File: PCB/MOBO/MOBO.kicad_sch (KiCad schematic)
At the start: 10 parts, among them J101 COMP_OUT, J102 COMP_5V, J103 COMP_GND, J104 RPi_GPio, J105 JST_02, J106 RPi_SDA0, J107 RPi_TV, J108 RPi_D-, J109 RPi_D+, J110 RPi_SCL0

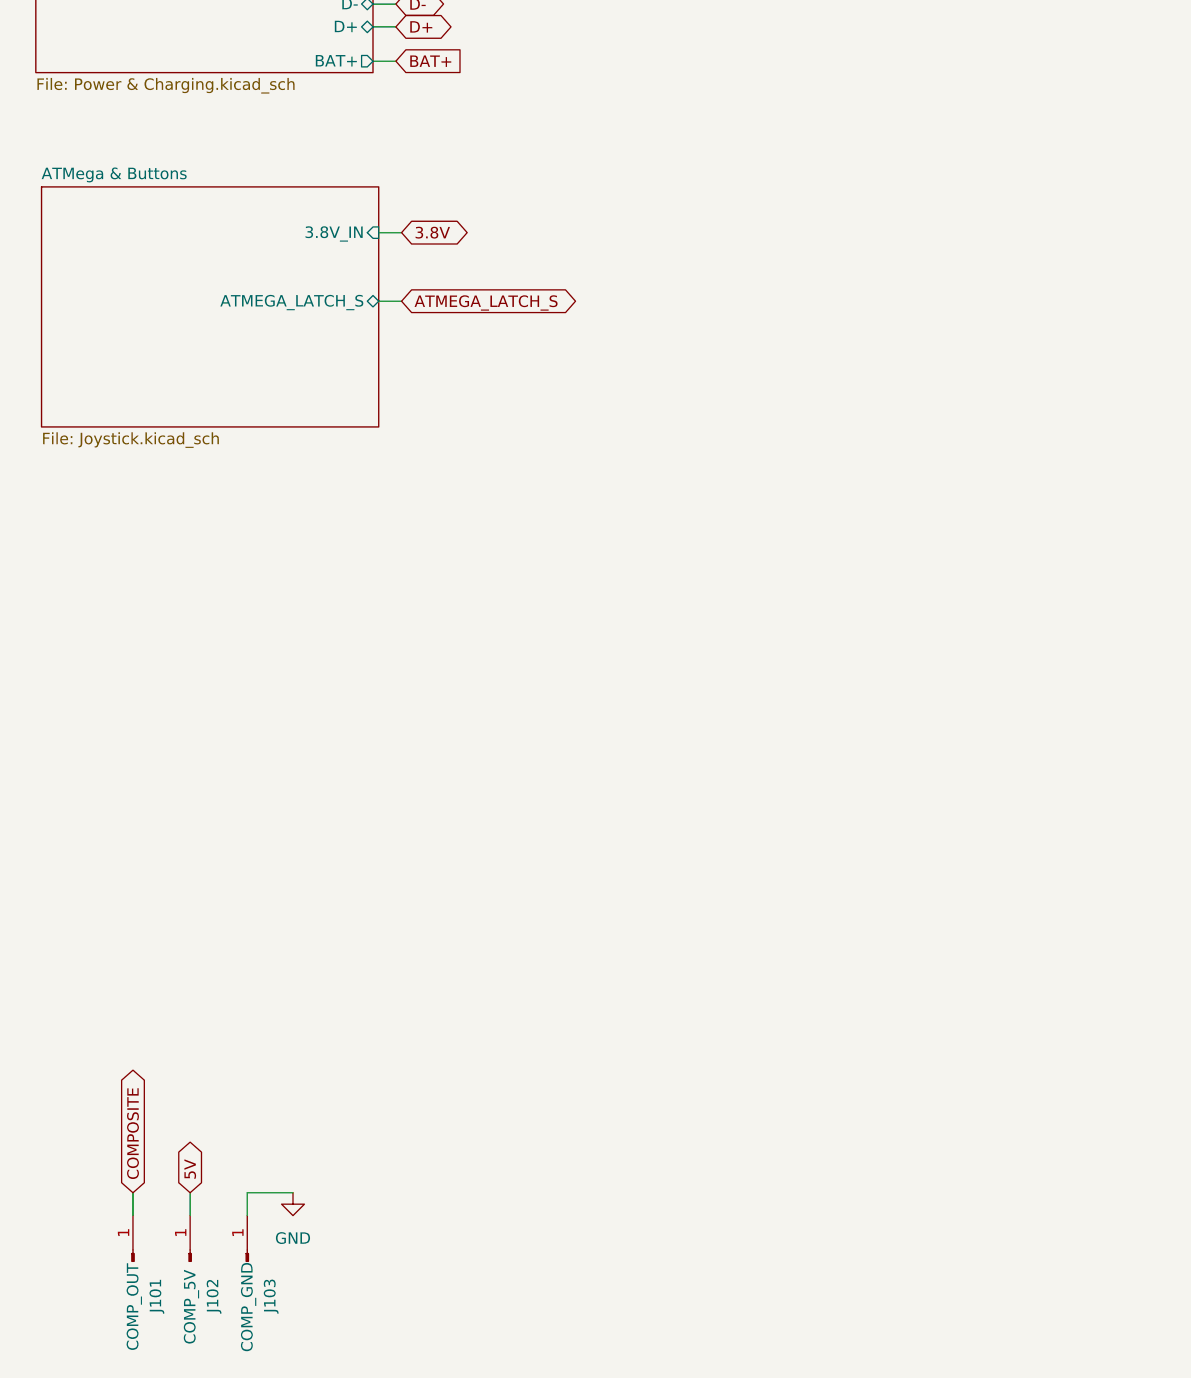
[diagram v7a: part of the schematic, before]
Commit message: schematic cleanup Added:  - Power flags  - Fixed loose connections
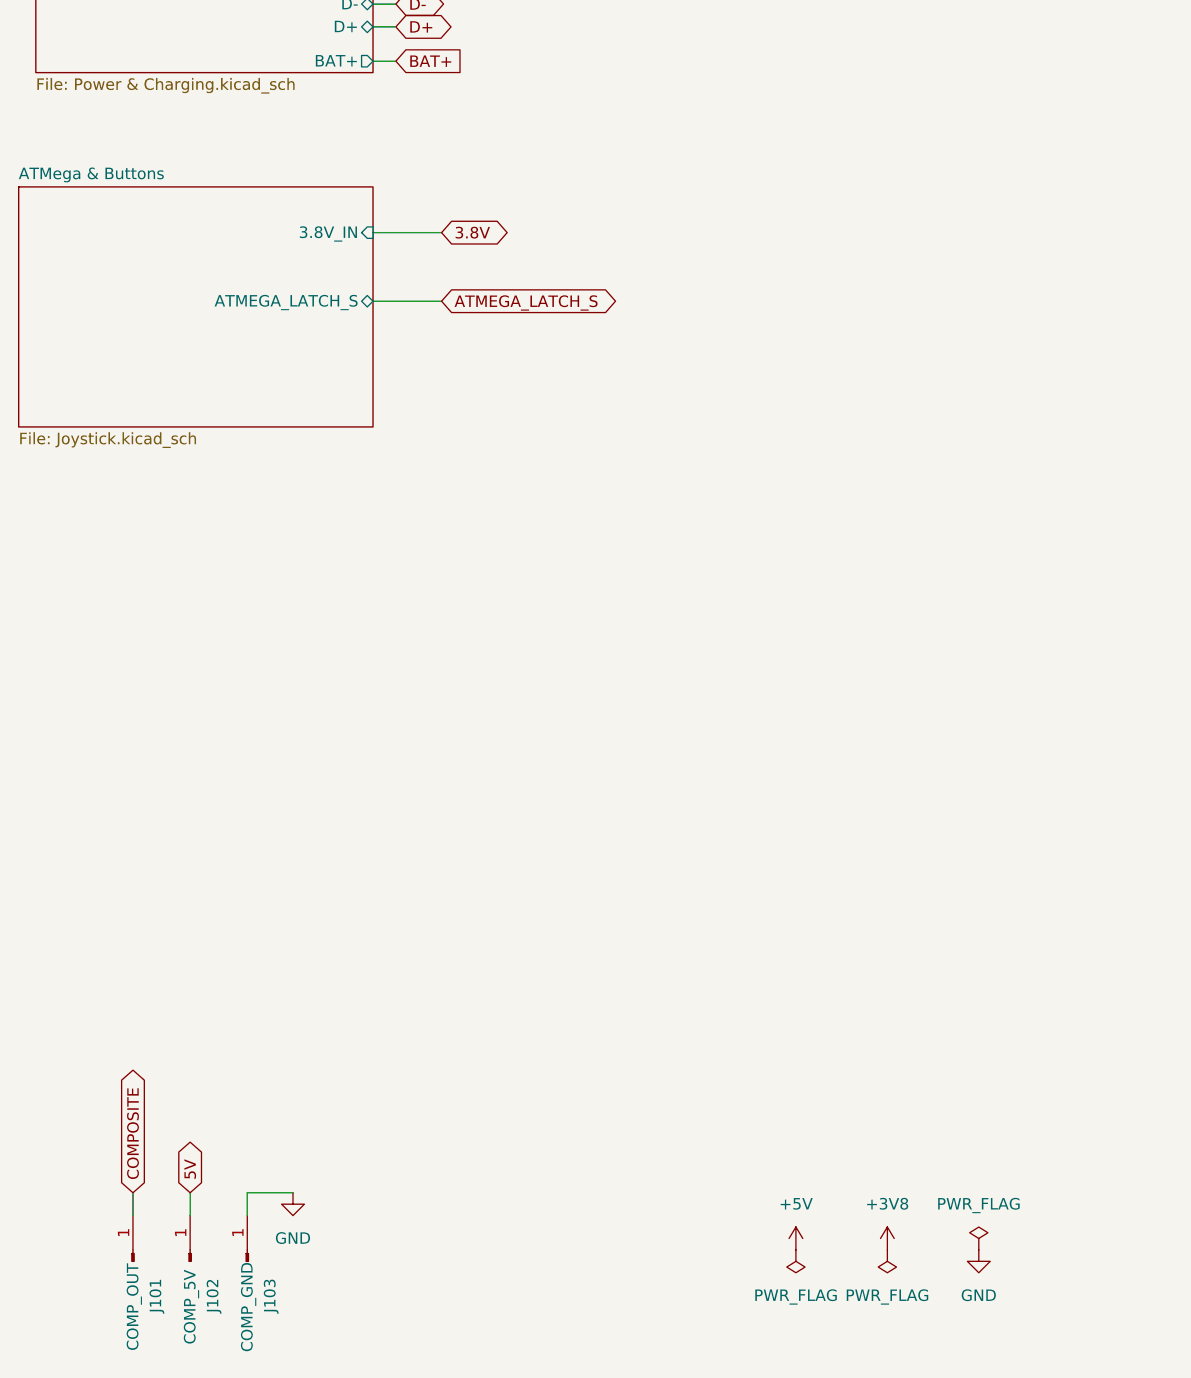
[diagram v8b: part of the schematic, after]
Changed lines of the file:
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@@
     (stroke (width 0) (type default))
   )
-  (wire (pts (xy 60.325 76.2) (xy 62.865 76.2))
+  (wire (pts (xy 59.69 76.2) (xy 67.31 76.2))
     (stroke (width 0) (type default))
   )
@@
     (stroke (width 0) (type default))
   )
-  (wire (pts (xy 60.325 68.58) (xy 62.865 68.58))
+  (wire (pts (xy 59.69 68.58) (xy 67.31 68.58))
     (stroke (width 0) (type default))
   )
@@
     )
   )
-  (global_label "ATMEGA_LATCH_S" (shape bidirectional) (at 62.865 76.2 0) (fields_autoplaced)
-    (effects (font (size 1.27 1.27)) (justify left))
-    (property "Intersheetrefs" "${INTERSHEET_REFS}" (at 82.8062 76.2 0)
+  (global_label "ATMEGA_LATCH_S" (shape bidirectional) (at 67.31 76.2 0) (fields_autoplaced)
+    (effects (font (size 1.27 1.27)) (justify left))
+    (property "Intersheetrefs" "${INTERSHEET_REFS}" (at 87.2512 76.2 0)
       (effects (font (size 1.27 1.27)) (justify left) hide)
     )
@@
     )
   )
-  (global_label "3.8V" (shape bidirectional) (at 62.865 68.58 0) (fields_autoplaced)
-    (effects (font (size 1.27 1.27)) (justify left))
-    (property "Intersheetrefs" "${INTERSHEET_REFS}" (at 71.0739 68.58 0)
+  (global_label "3.8V" (shape bidirectional) (at 67.31 68.58 0) (fields_autoplaced)
+    (effects (font (size 1.27 1.27)) (justify left))
+    (property "Intersheetrefs" "${INTERSHEET_REFS}" (at 75.5189 68.58 0)
       (effects (font (size 1.27 1.27)) (justify left) hide)
     )
@@
     )
   )
+  (symbol (lib_id "power:GND") (at 127 181.61 0) (unit 1)
+    (in_bom yes) (on_board yes) (dnp no) (fields_autoplaced)
+    (property "Reference" "#PWR0106" (at 127 187.96 0)
+      (effects (font (size 1.27 1.27)) hide)
+    )
+    (property "Value" "GND" (at 127 186.69 0)
+      (effects (font (size 1.27 1.27)))
+    )
+    (property "Footprint" "" (at 127 181.61 0)
+      (effects (font (size 1.27 1.27)) hide)
+    )
+    (property "Datasheet" "" (at 127 181.61 0)
+      (effects (font (size 1.27 1.27)) hide)
+    )
+    (pin "1")
+    (instances
+      (project "MOBO"
+        (path "/2d62a3c1-c4f2-4921-9f6b-8dc8aef69d64"
+          (reference "#PWR0106") (unit 1)
+        )
+      )
+    )
+  )
   (symbol (lib_id "Connector:Conn_01x01_Male") (at 45.72 182.88 90) (unit 1)
     (in_bom yes) (on_board yes) (dnp no)
@@
     )
   )
+  (symbol (lib_id "power:PWR_FLAG") (at 106.68 181.61 180) (unit 1)
+    (in_bom yes) (on_board yes) (dnp no) (fields_autoplaced)
+    (property "Reference" "#FLG0102" (at 106.68 183.515 0)
+      (effects (font (size 1.27 1.27)) hide)
+    )
+    (property "Value" "PWR_FLAG" (at 106.68 186.69 0)
+      (effects (font (size 1.27 1.27)))
+    )
+    (property "Footprint" "" (at 106.68 181.61 0)
+      (effects (font (size 1.27 1.27)) hide)
+    )
+    (property "Datasheet" "~" (at 106.68 181.61 0)
+      (effects (font (size 1.27 1.27)) hide)
+    )
+    (pin "1")
+    (instances
+      (project "MOBO"
+        (path "/2d62a3c1-c4f2-4921-9f6b-8dc8aef69d64"
+          (reference "#FLG0102") (unit 1)
+        )
+      )
+    )
+  )
   (symbol (lib_id "power:GND") (at 257.81 57.15 0) (mirror y) (unit 1)
     (in_bom yes) (on_board yes) (dnp no) (fields_autoplaced)
@@
         (path "/2d62a3c1-c4f2-4921-9f6b-8dc8aef69d64"
           (reference "#PWR0103") (unit 1)
+        )
+      )
+    )
+  )
+  (symbol (lib_id "power:+3V8") (at 116.84 181.61 0) (unit 1)
+    (in_bom yes) (on_board yes) (dnp no) (fields_autoplaced)
+    (property "Reference" "#PWR0105" (at 116.84 185.42 0)
+      (effects (font (size 1.27 1.27)) hide)
+    )
+    (property "Value" "+3V8" (at 116.84 176.53 0)
+      (effects (font (size 1.27 1.27)))
+    )
+    (property "Footprint" "" (at 116.84 181.61 0)
+      (effects (font (size 1.27 1.27)) hide)
+    )
+    (property "Datasheet" "" (at 116.84 181.61 0)
+      (effects (font (size 1.27 1.27)) hide)
+    )
+    (pin "1")
+    (instances
+      (project "MOBO"
+        (path "/2d62a3c1-c4f2-4921-9f6b-8dc8aef69d64"
+          (reference "#PWR0105") (unit 1)
         )
       )
@@
     )
   )
+  (symbol (lib_id "power:PWR_FLAG") (at 116.84 181.61 180) (unit 1)
+    (in_bom yes) (on_board yes) (dnp no) (fields_autoplaced)
+    (property "Reference" "#FLG0103" (at 116.84 183.515 0)
+      (effects (font (size 1.27 1.27)) hide)
+    )
+    (property "Value" "PWR_FLAG" (at 116.84 186.69 0)
+      (effects (font (size 1.27 1.27)))
+    )
+    (property "Footprint" "" (at 116.84 181.61 0)
+      (effects (font (size 1.27 1.27)) hide)
+    )
+    (property "Datasheet" "~" (at 116.84 181.61 0)
+      (effects (font (size 1.27 1.27)) hide)
+    )
+    (pin "1")
+    (instances
+      (project "MOBO"
+        (path "/2d62a3c1-c4f2-4921-9f6b-8dc8aef69d64"
+          (reference "#FLG0103") (unit 1)
+        )
+      )
+    )
+  )
   (symbol (lib_id "Connector:Conn_01x01_Male") (at 269.24 69.85 180) (unit 1)
     (in_bom yes) (on_board yes) (dnp no)
@@
     )
   )
+  (symbol (lib_id "power:+5V") (at 106.68 181.61 0) (unit 1)
+    (in_bom yes) (on_board yes) (dnp no) (fields_autoplaced)
+    (property "Reference" "#PWR0104" (at 106.68 185.42 0)
+      (effects (font (size 1.27 1.27)) hide)
+    )
+    (property "Value" "+5V" (at 106.68 176.53 0)
+      (effects (font (size 1.27 1.27)))
+    )
+    (property "Footprint" "" (at 106.68 181.61 0)
+      (effects (font (size 1.27 1.27)) hide)
+    )
+    (property "Datasheet" "" (at 106.68 181.61 0)
+      (effects (font (size 1.27 1.27)) hide)
+    )
+    (pin "1")
+    (instances
+      (project "MOBO"
+        (path "/2d62a3c1-c4f2-4921-9f6b-8dc8aef69d64"
+          (reference "#PWR0104") (unit 1)
+        )
+      )
+    )
+  )
   (symbol (lib_id "power:GND") (at 50.8 175.26 0) (unit 1)
     (in_bom yes) (on_board yes) (dnp no) (fields_autoplaced)
@@
     )
   )
+  (symbol (lib_id "power:PWR_FLAG") (at 127 181.61 0) (unit 1)
+    (in_bom yes) (on_board yes) (dnp no) (fields_autoplaced)
+    (property "Reference" "#FLG0101" (at 127 179.705 0)
+      (effects (font (size 1.27 1.27)) hide)
+    )
+    (property "Value" "PWR_FLAG" (at 127 176.53 0)
+      (effects (font (size 1.27 1.27)))
+    )
+    (property "Footprint" "" (at 127 181.61 0)
+      (effects (font (size 1.27 1.27)) hide)
+    )
+    (property "Datasheet" "~" (at 127 181.61 0)
+      (effects (font (size 1.27 1.27)) hide)
+    )
+    (pin "1")
+    (instances
+      (project "MOBO"
+        (path "/2d62a3c1-c4f2-4921-9f6b-8dc8aef69d64"
+          (reference "#FLG0101") (unit 1)
+        )
+      )
+    )
+  )
   (symbol (lib_id "Connector:Conn_01x01_Male") (at 269.24 64.77 180) (unit 1)
     (in_bom yes) (on_board yes) (dnp no)
@@
     )
   )
-  (sheet (at 22.86 63.5) (size 37.465 26.67) (fields_autoplaced)
+  (sheet (at 20.32 63.5) (size 39.37 26.67) (fields_autoplaced)
     (stroke (width 0.1524) (type solid))
     (fill (color 0 0 0 0.0000))
-    (property "Sheetname" "ATMega & Buttons" (at 22.86 62.7884 0)
+    (property "Sheetname" "ATMega & Buttons" (at 20.32 62.7884 0)
       (effects (font (size 1.27 1.27)) (justify left bottom))
     )
-    (property "Sheetfile" "Joystick.kicad_sch" (at 22.86 90.7546 0)
+    (property "Sheetfile" "Joystick.kicad_sch" (at 20.32 90.7546 0)
       (effects (font (size 1.27 1.27)) (justify left top))
     )
-    (pin "3.8V_IN" input (at 60.325 68.58 0)
+    (pin "3.8V_IN" input (at 59.69 68.58 0)
       (effects (font (size 1.27 1.27)) (justify right))
     )
-    (pin "ATMEGA_LATCH_S" bidirectional (at 60.325 76.2 0)
+    (pin "ATMEGA_LATCH_S" bidirectional (at 59.69 76.2 0)
       (effects (font (size 1.27 1.27)) (justify right))
     )
